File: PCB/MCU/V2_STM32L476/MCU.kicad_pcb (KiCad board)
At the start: 2 copper layers, 40 x 46.2 mm, 40 parts, among them IC2 LTC4311CSC6#TRPBF, J1 Conn_02x06_Odd_Even, J2 Conn_02x06_Odd_Even, J4 Conn_01x04_Pin, J5 RESET, J6 Conn_01x04_Pin, Q1 PJE8408_R1_00001, Q2 PJE8408_R1_00001, U1 MB85RS2MTAPNF-G-BDERE1, U3 MAX6372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

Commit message: mac:working on the stm32l476 mcu board
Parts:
- removed C7: 0.01uF, Capacitor_SMD:C_0402_1005Metric_Pad0.74x0.62mm_HandSolder
- removed J4: Conn_01x04_Pin, Connector_PinHeader_2.54mm:PinHeader_1x04_P2.54mm_Vertical
- removed R14, R15: 499K, Resistor_SMD:R_0402_1005Metric_Pad0.72x0.64mm_HandSolder
- removed R4: 10K, Resistor_SMD:R_0402_1005Metric
- removed R5, R6: 27, Resistor_SMD:R_0402_1005Metric_Pad0.72x0.64mm_HandSolder
- removed TP1: BAT_TP, TestPoint:TestPoint_Pad_1.0x1.0mm
- added C17: 0.1uF, Capacitor_SMD:C_0402_1005Metric_Pad0.74x0.62mm_HandSolder, F.Cu at (141.3, 94.5)
- added C18: 0.1uF, Capacitor_SMD:C_0402_1005Metric_Pad0.74x0.62mm_HandSolder, F.Cu at (153.0, 98.7)
- added C19: 0.1uF, Capacitor_SMD:C_0402_1005Metric_Pad0.74x0.62mm_HandSolder, F.Cu at (150.4, 108.3)
- added C20: 0.1uF, Capacitor_SMD:C_0402_1005Metric_Pad0.74x0.62mm_HandSolder, F.Cu at (142.3, 110.4)
- added C21: 0.1uF, Capacitor_SMD:C_0402_1005Metric_Pad0.74x0.62mm_HandSolder, F.Cu at (137.8, 105.3)
- added C22: 18pF, Capacitor_SMD:C_0402_1005Metric_Pad0.74x0.62mm_HandSolder, F.Cu at (133.4, 100.3)
- added C23: 18pF, Capacitor_SMD:C_0402_1005Metric_Pad0.74x0.62mm_HandSolder, F.Cu at (139.7, 95.6)
- added C24: 18pF, Capacitor_SMD:C_0402_1005Metric_Pad0.74x0.62mm_HandSolder, F.Cu at (134.6, 95.6)
- added C26: 18pF, Capacitor_SMD:C_0402_1005Metric_Pad0.74x0.62mm_HandSolder, F.Cu at (133.4, 105.6)
- added D2: Green, LED_SMD:LED_0402_1005Metric_Pad0.77x0.64mm_HandSolder, F.Cu at (139.1, 115.8)
- added R16: 0Ω, PCM_JLCPCB:R_0402, F.Cu at (137.3, 98.7)
- added R22: 10kΩ, Resistor_SMD:R_0402_1005Metric_Pad0.72x0.64mm_HandSolder, F.Cu at (137.1, 114.7)
- added R25: 10kΩ, Resistor_SMD:R_0603_1608Metric_Pad0.98x0.95mm_HandSolder, F.Cu at (144.2, 94.9)
- added U7: STM32L476RGT6, Package_QFP:LQFP-64_10x10mm_P0.5mm, F.Cu at (145.1, 102.5)
- added Y2: 32KHz, Crystal:Crystal_SMD_3215-2Pin_3.2x1.5mm, F.Cu at (137.1, 95.6)
- C16: moved to F.Cu
- R1, R2: value 4.7K -> 4.7kΩ; footprint Resistor_SMD:R_0402_1005Metric_Pad0.72x0.64mm_HandSolder -> PCM_JLCPCB:R_0402
- moved JP1 8.20 mm to (139.9, 90.3), turned to -90 degrees
- moved C3 7.09 mm to (157.0, 111.1), turned to 0 degrees
- moved C11 6.99 mm to (159.9, 89.6)
- moved R21 6.70 mm to (157.5, 94.9)
- moved R18 6.66 mm to (164.3, 96.4), turned to 180 degrees
- moved R17 6.66 mm to (157.7, 96.4)
- moved Q1 6.66 mm to (162.2, 97.2)
- moved Q2 6.66 mm to (159.8, 97.2)
- moved U5 6.64 mm to (161.5, 92.8)
- moved C10 6.41 mm to (143.6, 89.0)
- moved U3 6.41 mm to (144.1, 91.6)
- moved C16 6.17 mm to (161.3, 89.6)
- moved R9 5.14 mm to (137.4, 90.3), turned to 180 degrees
- moved C14 4.99 mm to (156.0, 89.0)
- moved C9 4.98 mm to (150.8, 91.9)
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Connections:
- C1 pad 1: VCC -> +3.3V
- C10 pad 1: VCC -> +3.3V
- C3 pad 1: VCC -> +3.3V
- C9 pad 2: VCC -> +3.3V
- IC2 pad 1: VCC -> +3.3V
- IC2 pad 4: /SCL -> I2C2_SCL
- IC2 pad 6: /SDA -> I2C2_SDA
- J1 pad 11: /SDA -> I2C2_SDA
- J1 pad 12: /SCL -> I2C2_SCL
- J2 pad 3: /MOSI -> SPI1_MOSI
- J2 pad 5: /SCK -> SPI1_SCK
- J2 pad 9: /MISO -> SPI1_MISO
- J6 pad 1: +5V -> +3.3V
- J6 pad 2: Net-(J6-Pin_2) -> SWDCLK
- J6 pad 3: Net-(J6-Pin_3) -> SWDIO
- Q1 pad 3: /SDA -> I2C2_SDA
- Q2 pad 3: /SCL -> I2C2_SCL
- R1 pad 1: /SCL -> +3.3V
- R1 pad 2: VCC -> I2C2_SCL
- R12 pad 2: VCC -> +3.3V
- R13 pad 2: VCC -> +3.3V
- R2 pad 1: /SDA -> +3.3V
- R2 pad 2: VCC -> I2C2_SDA
- R9 pad 2: /~{RESET} -> NRST
- U1 pad 8: VCC -> +3.3V
- U3 pad 1: /RXLED -> /WDI
- U3 pad 4: VCC -> +3.3V
- U3 pad 5: VCC -> +3.3V
- U3 pad 6: VCC -> +3.3V
- U3 pad 8: VCC -> +3.3V
- U4 pad 5: VCC -> +3.3V
- U6 pad 3: /VBAT -> /1V8_EN
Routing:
- net +3.3V: track 0.00 -> 116.4 mm, vias 0 -> 10
- net I2C2_SCL: track 0.00 -> 37.4 mm, vias 0 -> 3
- net I2C2_SDA: track 0.00 -> 36.9 mm, vias 0 -> 3
- net VCC: track 32.9 -> 0.00 mm, vias 1 -> 0
- net /SCL: track 27.5 -> 0.00 mm
- net /VBAT: track 0.00 -> 25.0 mm
- net SWDCLK: track 0.00 -> 20.7 mm
- net SWDIO: track 0.00 -> 18.3 mm
- net NRST: track 0.00 -> 15.4 mm, vias 0 -> 2
- net SPI1_MOSI: track 0.00 -> 13.1 mm
- net SPI1_SCK: track 0.00 -> 11.9 mm
- net Net-(U7-PC14-OSC32_IN(PC14)): track 0.00 -> 10.7 mm
- net Net-(U7-PC15-OSC32_OUT(PC15)): track 0.00 -> 10.1 mm
- net PA3: track 0.00 -> 8.81 mm
- net +1V8: track 28.0 -> 19.7 mm, vias 1 -> 2
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- added copper zone on In1.Cu, net GND
- added copper zone on In2.Cu, net GND
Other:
- copper layers 2 -> 4
- board text removed: "X"
- board text removed: "Y"
- board text removed: "Z"

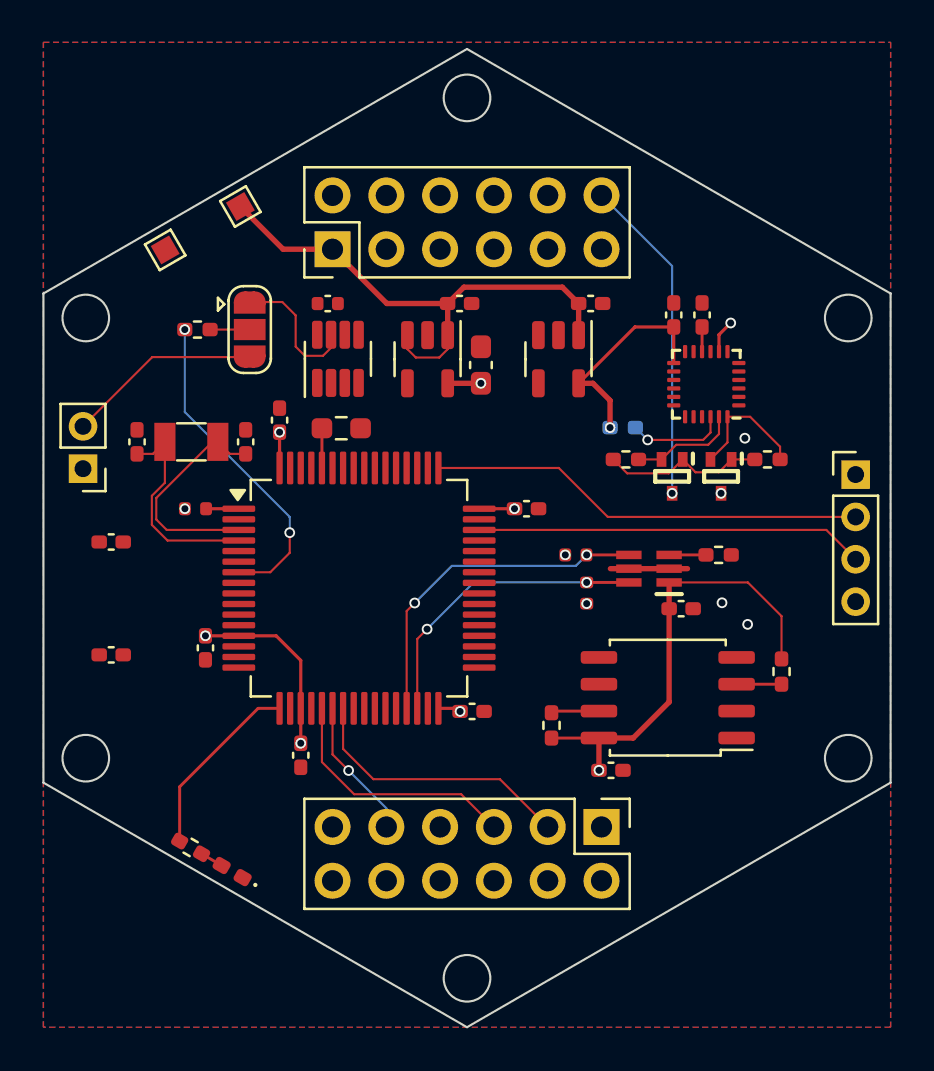
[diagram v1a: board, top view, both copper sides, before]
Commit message: mac: finishing the L476 mcu board
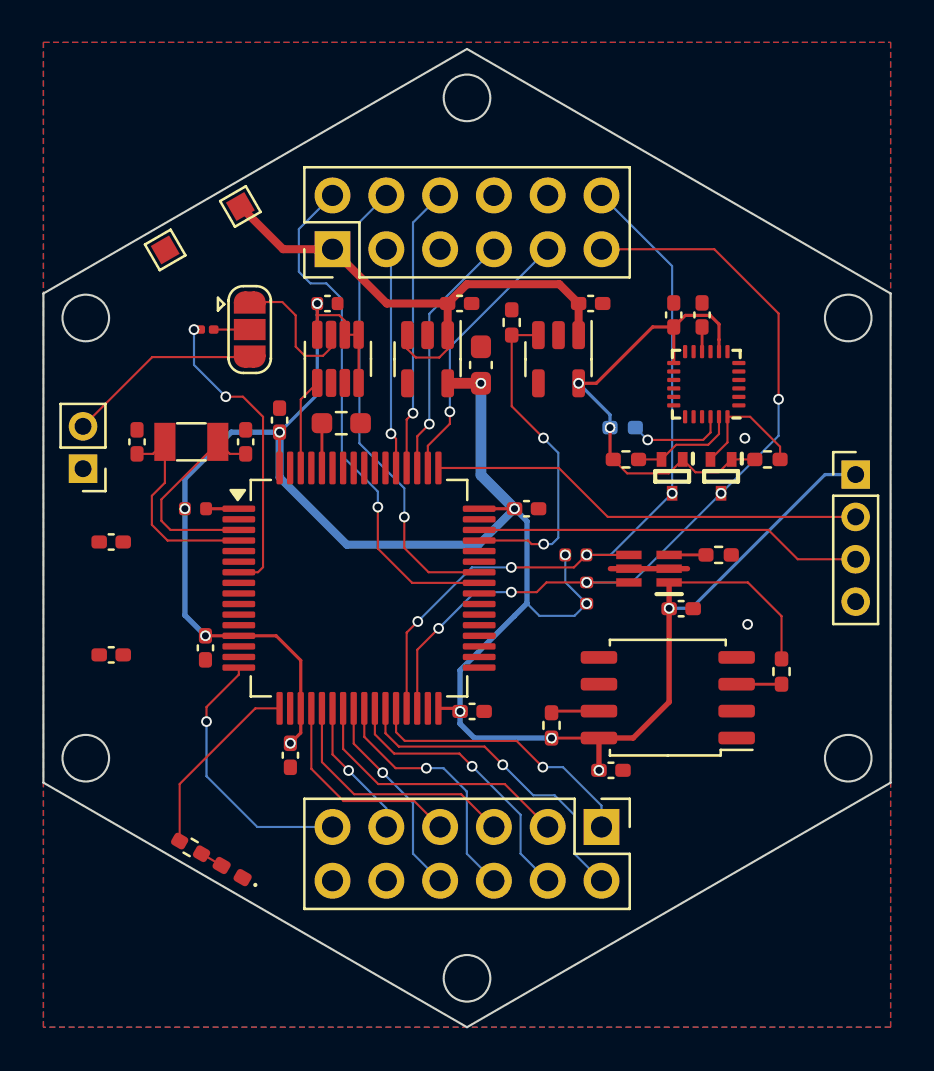
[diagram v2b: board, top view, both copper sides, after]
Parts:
- added R4: 10K, Resistor_SMD:R_0402_1005Metric_Pad0.72x0.64mm_HandSolder, F.Cu at (152.3, 89.9)
- R9: value 330 -> 0; footprint Resistor_SMD:R_0402_1005Metric_Pad0.72x0.64mm_HandSolder -> Resistor_SMD:R_0201_0603Metric
- moved C20 0.49 mm to (141.8, 110.4)
- moved R9 0.45 mm to (137.9, 90.3)
- moved R25 0.24 mm to (144.2, 94.7)
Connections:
- J1 pad 2: /D8 -> PA8
- J1 pad 3: /A5 -> SPI3_MOSI
- J1 pad 4: /A3 -> PA9
- J1 pad 6: /A2 -> SPI3_MISO
- J1 pad 7: /RXD -> SPI3_SCK
- J1 pad 9: /TXD -> SPI3_CS
- J2 pad 1: /D12 -> PB2
- J2 pad 11: /D4 -> PA2
- J2 pad 2: /D10 -> PB1
- J2 pad 4: /D1 -> PB0
- J2 pad 6: /D3 -> PC5
- J2 pad 7: /D2 -> SPI1_CS
- J2 pad 8: /A4 -> PC4
- U3 pad 1: /WDI -> PB9
- U6 pad 3: /1V8_EN -> PA12
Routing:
- net PA8: track 0.00 -> 24.8 mm, vias 0 -> 1
- net PA9: track 0.00 -> 22.1 mm, vias 0 -> 1
- net PA12: track 0.00 -> 15.7 mm, vias 0 -> 2
- net PB1: track 0.00 -> 15.3 mm, vias 0 -> 1
- net SPI3_MISO: track 0.00 -> 13.5 mm, vias 0 -> 1
- net PB0: track 0.00 -> 13.3 mm, vias 0 -> 1
- net PB2: track 0.00 -> 13.3 mm, vias 0 -> 1
- net PA2: track 0.00 -> 12.7 mm, vias 0 -> 1
- net SPI3_CS: track 0.00 -> 12.7 mm, vias 0 -> 1
- net PC5: track 0.00 -> 12.0 mm, vias 0 -> 1
- net SPI3_SCK: track 0.00 -> 11.8 mm, vias 0 -> 1
- net SPI3_MOSI: track 0.00 -> 10.5 mm, vias 0 -> 1
- net SPI1_CS: track 0.00 -> 10.1 mm
- net PC4: track 0.00 -> 9.83 mm, vias 0 -> 1
- net I2C2_SDA: track 36.9 -> 41.4 mm, vias 3 -> 5
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- removed copper zone on In1.Cu, net GND
- removed copper zone on In2.Cu, net GND
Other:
- copper layers 4 -> 2

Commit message: mac: finishing the L476 mcu board
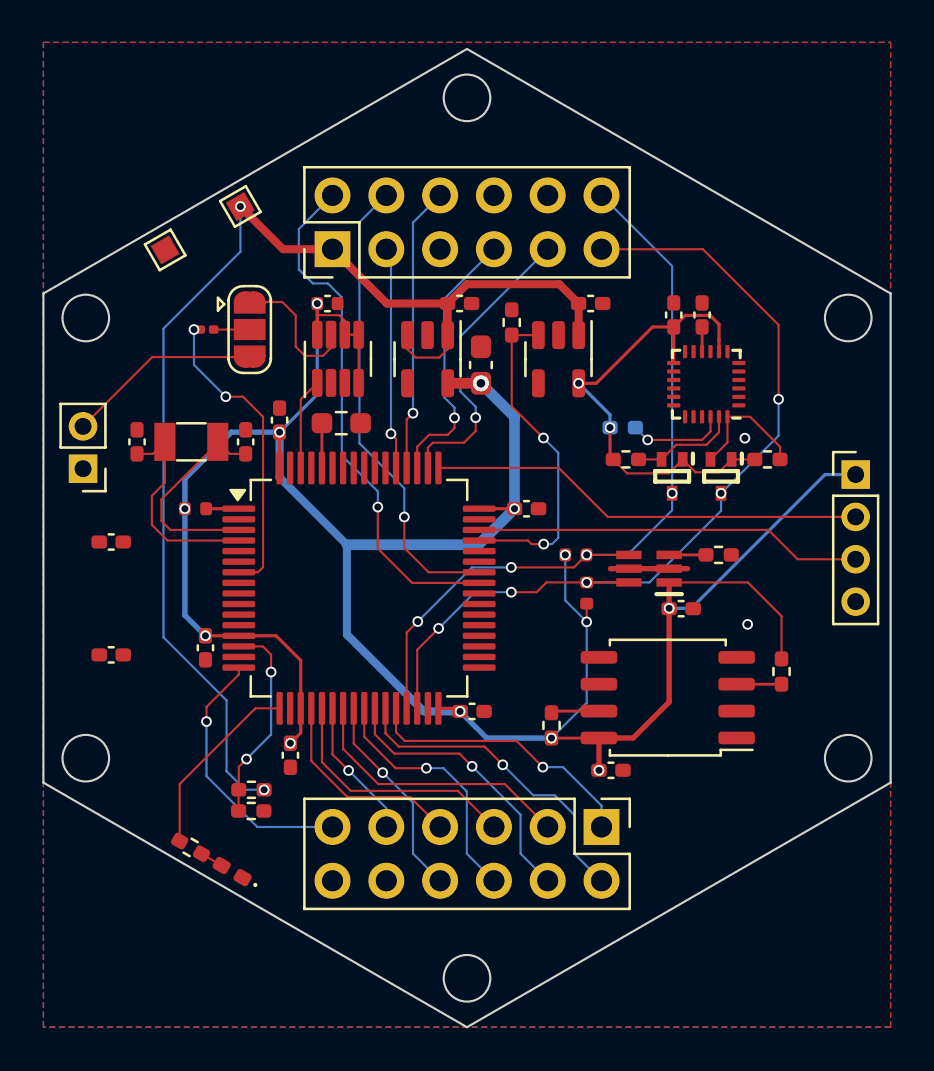
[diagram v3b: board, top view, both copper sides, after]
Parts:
- added R5: 10K, Resistor_SMD:R_0402_1005Metric_Pad0.72x0.64mm_HandSolder, F.Cu at (140.0, 112.0)
- added R6: 10K, Resistor_SMD:R_0402_1005Metric_Pad0.72x0.64mm_HandSolder, F.Cu at (140.0, 113.0)
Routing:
- net /VBAT: track 25.2 -> 56.7 mm, vias 0 -> 2
- net PA0: track 0.00 -> 9.70 mm, vias 0 -> 2
- net +3.3V: track 118.6 -> 122.8 mm
- net SPI3_CS: track 12.7 -> 14.1 mm
- net SPI3_SCK: track 11.8 -> 12.7 mm

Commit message: pc:finished L476 MCU board
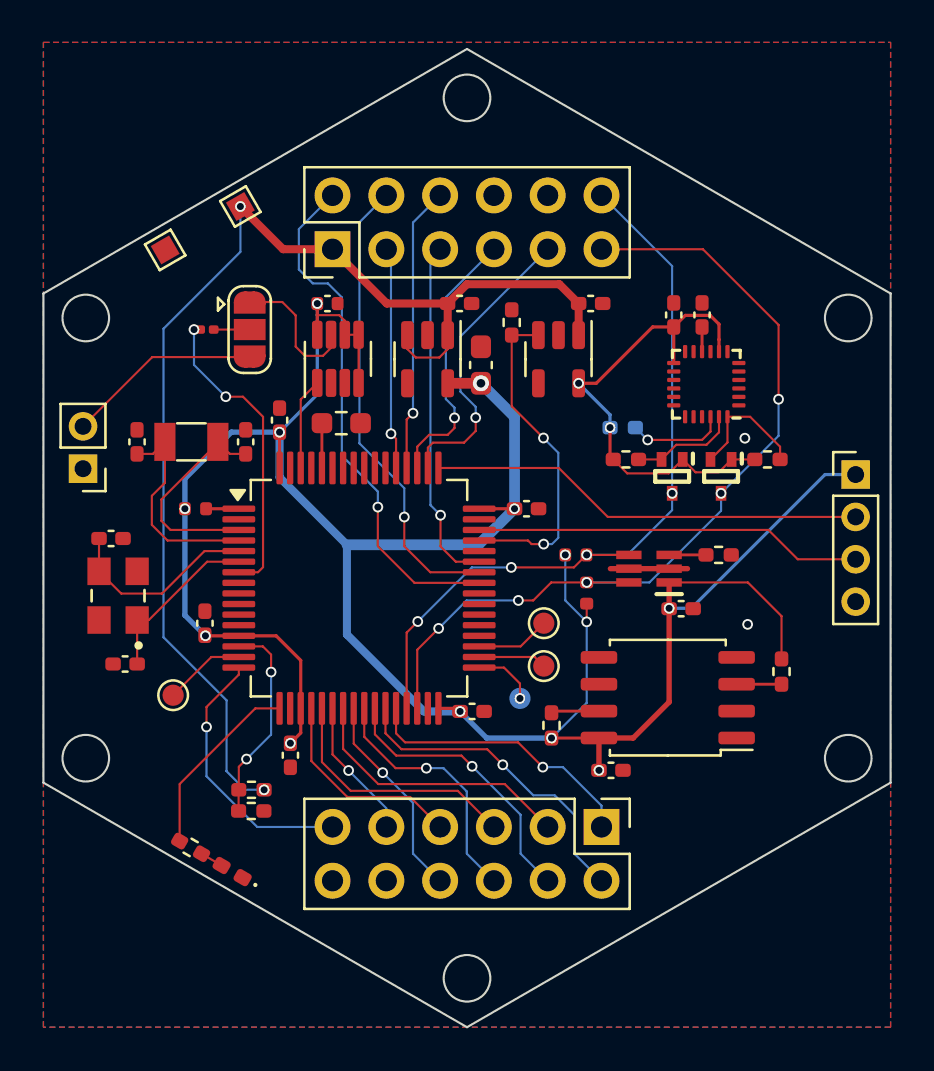
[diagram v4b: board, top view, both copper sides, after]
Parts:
- added TP1: TestPoint, TestPoint:TestPoint_Pad_D1.0mm, F.Cu at (136.3, 107.5)
- added TP4: TestPoint, TestPoint:TestPoint_Pad_D1.0mm, B.Cu at (152.7, 107.7)
- added TP5: TestPoint, TestPoint:TestPoint_Pad_D1.0mm, F.Cu at (153.8, 106.1)
- added TP6: TestPoint, TestPoint:TestPoint_Pad_D1.0mm, F.Cu at (153.8, 104.1)
- added Y3: ECS-160-12-33-AGN-TR3, Mylib:XTAL_ECS-160-12-33-AGN-TR3, F.Cu at (133.7, 102.8)
- moved C21 1.16 mm to (137.8, 104.1), turned to 90 degrees
- moved C26 0.79 mm to (134.0, 106.0), turned to 180 degrees
- moved C22 0.17 mm to (133.4, 100.1)
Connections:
- J1 pad 5: /VBUS -> PA10
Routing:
- net PA10: track 0.00 -> 16.5 mm, vias 0 -> 1
- net Net-(U7-PH0-OSC_IN(PH0)): track 0.00 -> 9.42 mm
- net Net-(U7-PH1-OSC_OUT(PH1)): track 0.00 -> 8.02 mm
- net PA1: track 0.00 -> 3.85 mm
- net PB14: track 0.00 -> 3.50 mm
- net PB13: track 0.00 -> 3.23 mm
- net PB12: track 0.00 -> 2.94 mm, vias 0 -> 1
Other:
- board text added: "Fangzheng Liu MIT Media Lab"
- board text added: "HexSense L476_MCU"
- board text removed: "Fangzhegn Liu MIT Media Lab fzliu@mit.edu"
- board text removed: "HexSense Canary Islands"
